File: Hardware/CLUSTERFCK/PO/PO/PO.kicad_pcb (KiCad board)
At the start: 2 copper layers, 2 parts, among them J1 Conn_02x08_Counter_Clockwise, J2 Conn_02x20_Counter_Clockwise

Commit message: 0061|1h|PO Module Versuch 2
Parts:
- J1: value Conn_02x08_Counter_Clockwise -> Conn_02x14_Counter_Clockwise; footprint Connector_PinHeader_2.54mm:PinHeader_2x08_P2.54mm_Vertical_SMD -> Connector_PinHeader_2.54mm:PinHeader_2x14_P2.54mm_Horizontal
- moved J1 19.9 mm to (94.4, 75.1), turned to 0 degrees
- moved J2 0.22 mm to (29.6, 116.7)
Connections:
- J1 pad 1: GND -> /ADDR0
- J1 pad 10: /DATA7 -> /ADDR9
- J1 pad 11: EXT0 -> /ADDR10
- J1 pad 12: EXT1 -> /ADDR11
- J1 pad 13: EXT2 -> HLT
- J1 pad 14: IRPT -> +5V
- J1 pad 15: HLT -> GND
- J1 pad 16: +5V -> CLK
- J1 pad 2: CLK -> /ADDR1
- J1 pad 3: /DATA0 -> /ADDR2
- J1 pad 4: /DATA1 -> /ADDR3
- J1 pad 5: /DATA2 -> /ADDR4
- J1 pad 6: /DATA3 -> /ADDR5
- J1 pad 7: /DATA4 -> /ADDR6
- J1 pad 8: /DATA5 -> /ADDR7
- J1 pad 9: /DATA6 -> /ADDR8
- J2 pad 10: /DATA7 -> DATA
- J2 pad 17: no_connect_31 -> no_connect_30
- J2 pad 18: no_connect_32 -> no_connect_31
- J2 pad 23: /ADDR0 -> /ADDR11
- J2 pad 24: /ADDR1 -> /ADDR10
- J2 pad 25: /ADDR2 -> /ADDR9
- J2 pad 26: /ADDR3 -> /ADDR8
- J2 pad 27: /ADDR4 -> /ADDR7
- J2 pad 28: /ADDR5 -> /ADDR6
- J2 pad 29: /ADDR6 -> /ADDR5
- J2 pad 30: /ADDR7 -> /ADDR4
- J2 pad 31: /ADDR8 -> /ADDR3
- J2 pad 32: /ADDR9 -> /ADDR2
- J2 pad 33: /ADDR10 -> /ADDR1
- J2 pad 34: /ADDR11 -> /ADDR0
- J2 pad 35: no_connect_33 -> no_connect_32
- J2 pad 36: no_connect_34 -> no_connect_33
- J2 pad 37: no_connect_35 -> no_connect_34
- J2 pad 38: no_connect_36 -> no_connect_35
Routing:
- net /DATA7: track 87.3 -> 0.00 mm, vias 2 -> 0
- net DATA: track 0.00 -> 72.5 mm
- net /ADDR6: track 0.00 -> 68.1 mm
- net /ADDR10: track 0.00 -> 68.1 mm
- net /ADDR1: track 0.00 -> 68.0 mm
- net /ADDR8: track 0.00 -> 67.9 mm
- net /ADDR7: track 0.00 -> 67.9 mm
- net /ADDR4: track 0.00 -> 67.9 mm
- net /ADDR3: track 0.00 -> 67.9 mm
- net /ADDR2: track 0.00 -> 67.9 mm
- net /ADDR11: track 0.00 -> 67.9 mm
- net /ADDR9: track 0.00 -> 67.9 mm
- net /ADDR5: track 0.00 -> 67.9 mm
- net /ADDR0: track 0.00 -> 65.7 mm
- net IRPT: track 112.9 -> 78.5 mm, vias 0 -> 1
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- added copper zone on F.Cu, net /ADDR0
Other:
- board outline added: 120.8 x 71.8 mm

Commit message: 0062 | 0 | review PO 2
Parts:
- J1: footprint Connector_PinHeader_2.54mm:PinHeader_2x14_P2.54mm_Horizontal -> Connector_PinHeader_2.54mm:PinHeader_2x14_P2.54mm_Vertical
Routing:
- net /ADDR0: track 65.7 -> 67.9 mm
- removed copper zone on F.Cu, net /ADDR0
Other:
- board text added: "Parallel Output Module"
- board text added: "Tom Schädler 2020"

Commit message: 0063 | 0,1h | PO review 2.1
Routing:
- net /DATA3: track 77.4 -> 76.6 mm
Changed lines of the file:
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@@
   (segment (start 28.1 112.92) (end 80.23 112.92) (width 0.2) (layer "F.Cu") (net 11))
   (segment (start 26.96 111.78) (end 28.1 112.92) (width 0.2) (layer "F.Cu") (net 11))
-  (segment (start 80.23 112.92) (end 80.59 113.28) (width 0.2) (layer "F.Cu") (net 11))
-  (via (at 80.59 113.28) (size 0.43) (drill 0.3) (layers "F.Cu" "B.Cu") (net 11))
+  (via (at 80.23 112.92) (size 0.43) (drill 0.3) (layers "F.Cu" "B.Cu") (net 11))
   (segment (start 95.764999 99.135001) (end 96.94 97.96) (width 0.2) (layer "B.Cu") (net 11))
-  (segment (start 80.6 113.27) (end 80.6 112.560998) (width 0.2) (layer "B.Cu") (net 11))
-  (segment (start 80.59 113.28) (end 80.6 113.27) (width 0.2) (layer "B.Cu") (net 11))
+  (segment (start 80.6 112.560998) (end 80.250998 112.91) (width 0.2) (layer "B.Cu") (net 11))
   (segment (start 80.6 112.560998) (end 94.025997 99.135001) (width 0.2) (layer "B.Cu") (net 11))
   (segment (start 94.025997 99.135001) (end 95.764999 99.135001) (width 0.2) (layer "B.Cu") (net 11))
@@
   (segment (start 26.96 114.32) (end 28.09 115.45) (width 0.2) (layer "B.Cu") (net 13))
   (segment (start 75.170998 115.45) (end 94.025997 96.595001) (width 0.2) (layer "B.Cu") (net 13))
-  (segment (start 25.784999 106.135999) (end 26.585997 105.335001) (width 0.2) (layer "F.Cu") (net 14))
   (segment (start 28.324999 115.495001) (end 26.395999 115.495001) (width 0.2) (layer "F.Cu") (net 14))
   (segment (start 26.395999 115.495001) (end 25.784999 114.884001) (width 0.2) (layer "F.Cu") (net 14))
-  (segment (start 26.585997 105.335001) (end 38.484999 105.335001) (width 0.2) (layer "F.Cu") (net 14))
-  (segment (start 41.98 101.84) (end 87.04 101.84) (width 0.2) (layer "F.Cu") (net 14))
-  (segment (start 87.04 101.84) (end 93.46 95.42) (width 0.2) (layer "F.Cu") (net 14))
+  (segment (start 25.784999 106.135999) (end 26.585997 105.335001) (width 0.2) (layer "F.Cu") (net 14))
+  (segment (start 84.484999 105.335001) (end 87.98 101.84) (width 0.2) (layer "F.Cu") (net 14))
+  (segment (start 87.98 101.84) (end 94.4 95.42) (width 0.2) (layer "F.Cu") (net 14))
+  (segment (start 26.585997 105.335001) (end 84.484999 105.335001) (width 0.2) (layer "F.Cu") (net 14))
+  (segment (start 29.5 114.32) (end 28.324999 115.495001) (width 0.2) (layer "F.Cu") (net 14))
   (segment (start 25.784999 114.884001) (end 25.784999 106.135999) (width 0.2) (layer "F.Cu") (net 14))
-  (segment (start 38.484999 105.335001) (end 41.98 101.84) (width 0.2) (layer "F.Cu") (net 14))
-  (segment (start 93.46 95.42) (end 94.4 95.42) (width 0.25) (layer "F.Cu") (net 14))
-  (segment (start 29.5 114.32) (end 28.324999 115.495001) (width 0.2) (layer "F.Cu") (net 14))
   (segment (start 28.15 100.27) (end 86.35 100.27) (width 0.2) (layer "F.Cu") (net 15))
   (segment (start 95.764999 94.055001) (end 96.94 92.88) (width 0.2) (layer "F.Cu") (net 15))
@@
   (segment (start 29.62 76.04) (end 29.96 76.38) (width 0.2) (layer "F.Cu") (net 33))
   (segment (start 29.96 76.38) (end 95.66 76.38) (width 0.2) (layer "F.Cu") (net 33))
-  (segment (start 92.3 74.89) (end 92.51 75.1) (width 0.2) (layer "F.Cu") (net 34))
-  (segment (start 28.230001 74.889999) (end 92.299999 74.889999) (width 0.2) (layer "F.Cu") (net 34))
-  (segment (start 92.299999 74.889999) (end 92.3 74.89) (width 0.2) (layer "F.Cu") (net 34))
-  (segment (start 92.51 75.1) (end 94.4 75.1) (width 0.2) (layer "F.Cu") (net 34))
+  (segment (start 94.189999 74.889999) (end 94.4 75.1) (width 0.2) (layer "F.Cu") (net 34))
   (segment (start 27.08 76.04) (end 28.230001 74.889999) (width 0.2) (layer "F.Cu") (net 34))
+  (segment (start 28.230001 74.889999) (end 94.189999 74.889999) (width 0.2) (layer "F.Cu") (net 34))
   (zone (net 16) (net_name "GND") (layer "B.Cu") (hatch edge 0.508)
     (connect_pads (clearance 0.508))

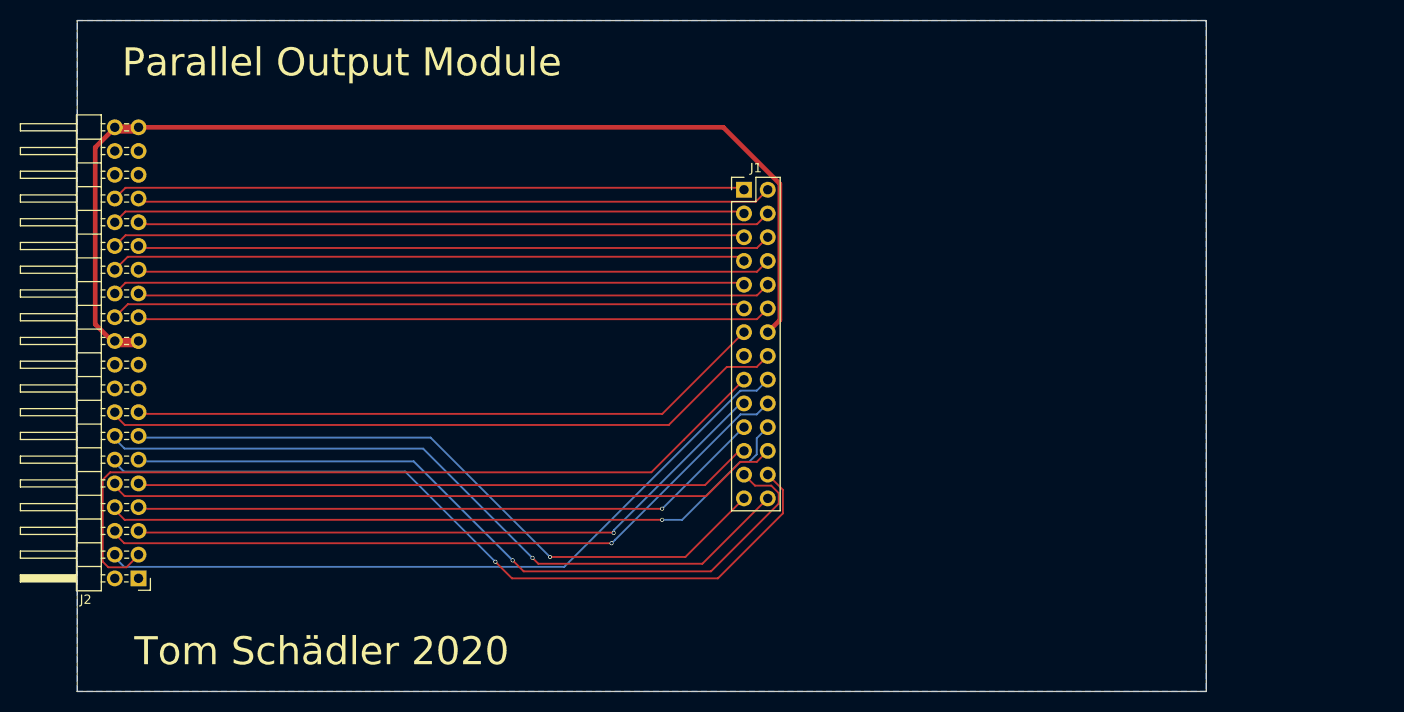
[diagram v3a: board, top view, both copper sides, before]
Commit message: quickfix PO width
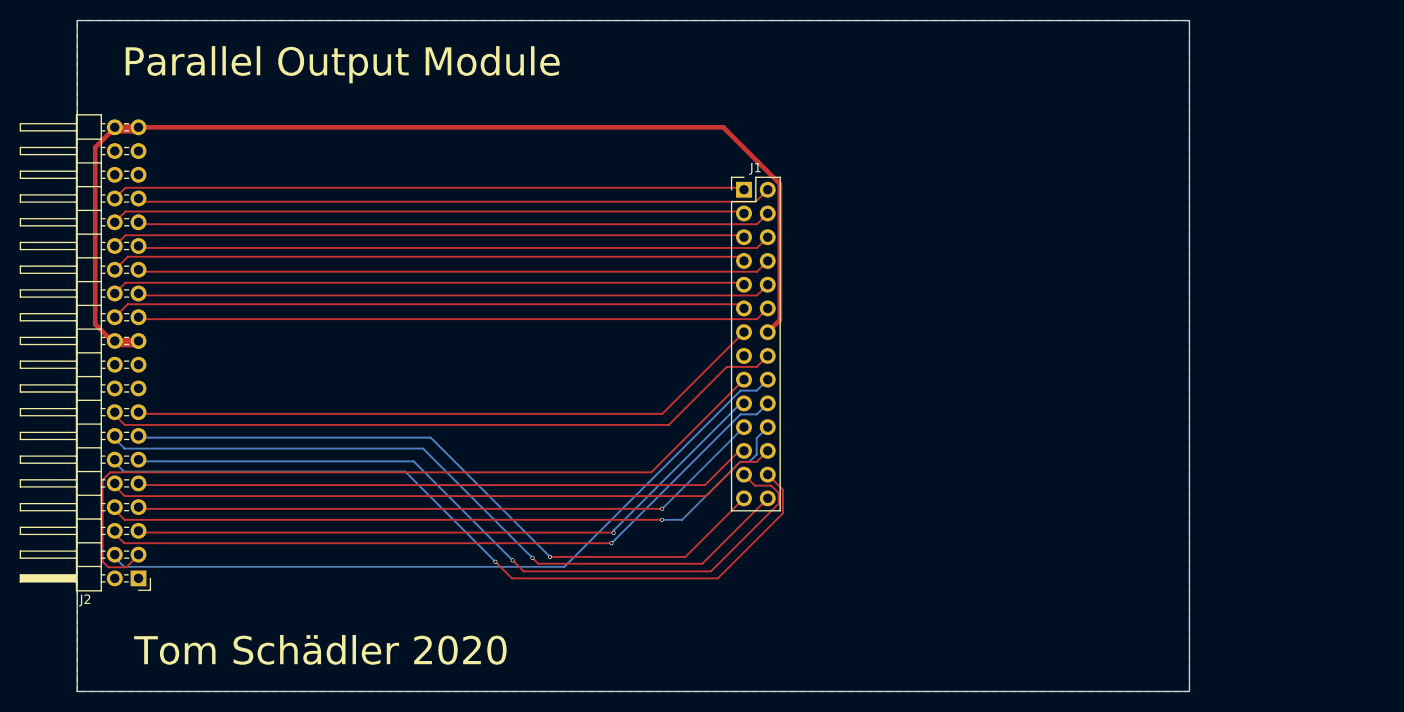
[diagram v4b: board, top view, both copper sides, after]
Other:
- board size 120.8 x 71.8 mm -> 119 x 71.8 mm
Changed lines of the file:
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@@
     )
   )
-  (gr_line (start 143.86 128.78) (end 143.86 57) (layer "Edge.Cuts") (width 0.1))
-  (gr_line (start 143.86 57) (end 23.06 57) (layer "Edge.Cuts") (width 0.1))
+  (gr_line (start 142.06 128.78) (end 142.06 57) (layer "Edge.Cuts") (width 0.1))
+  (gr_line (start 23.06 57) (end 142.06 57) (layer "Edge.Cuts") (width 0.1))
   (gr_line (start 23.06 57) (end 23.06 128.78) (layer "Edge.Cuts") (width 0.1))
-  (gr_line (start 23.06 128.78) (end 143.86 128.78) (layer "Edge.Cuts") (width 0.1))
+  (gr_line (start 23.06 128.78) (end 142.06 128.78) (layer "Edge.Cuts") (width 0.1))
   (gr_text "Tom Schädler 2020" (at 49.225 124.475) (layer "F.SilkS")
     (effects (font (size 3 3) (thickness 0.4)))
@@
     (polygon
       (pts
-        (xy 143.86 128.78)
+        (xy 142.06 128.78)
         (xy 23.06 128.78)
         (xy 23.06 57)
-        (xy 143.86 57)
+        (xy 142.06 57)
       )
     )

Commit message: 0066 | 6h | made holes in pcbs
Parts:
- added REF**: MountingHole_4.3mm_M4, MountingHole:MountingHole_4.3mm_M4, F.Cu at (52.9, 61.1)
- added REF**: MountingHole_4.3mm_M4, MountingHole:MountingHole_4.3mm_M4, F.Cu at (136.7, 62.3)
- added REF**: MountingHole_4.3mm_M4, MountingHole:MountingHole_4.3mm_M4, F.Cu at (28.6, 123.5)
- added REF**: MountingHole_4.3mm_M4, MountingHole:MountingHole_4.3mm_M4, F.Cu at (136.7, 123.5)
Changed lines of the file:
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@@
   (net 33 "/ADDR1")
   (net 34 "/ADDR0")
+  (footprint "MountingHole:MountingHole_4.3mm_M4" (layer "F.Cu")
+    (at 52.86 61.08)
+    (descr "Mounting Hole 4.3mm, no annular, M4")
+    (tags "mounting hole 4.3mm no annular m4")
+    (attr exclude_from_pos_files exclude_from_bom)
+    (fp_text reference "REF**" (at 0.09 -2.93) (layer "F.SilkS")
+      (effects (font (size 1 1) (thickness 0.15)))
+    )
+    (fp_text value "MountingHole_4.3mm_M4" (at 0 5.3) (layer "F.Fab")
+      (effects (font (size 1 1) (thickness 0.15)))
+    )
+    (fp_text user "${REFERENCE}" (at 0.3 0) (layer "F.Fab")
+      (effects (font (size 1 1) (thickness 0.15)))
+    )
+    (fp_circle (center 0 0) (end 4.3 0) (layer "Cmts.User") (width 0.15) (fill none))
+    (fp_circle (center 0 0) (end 4.55 0) (layer "F.CrtYd") (width 0.05) (fill none))
+    (pad "1" np_thru_hole circle (at 0 0) (size 4.3 4.3) (drill 4.3) (layers *.Cu *.Mask))
+  )
+  (footprint "MountingHole:MountingHole_4.3mm_M4" (layer "F.Cu")
+    (at 136.66 62.31)
+    (descr "Mounting Hole 4.3mm, no annular, M4")
+    (tags "mounting hole 4.3mm no annular m4")
+    (attr exclude_from_pos_files exclude_from_bom)
+    (fp_text reference "REF**" (at 0.09 -2.93) (layer "F.SilkS")
+      (effects (font (size 1 1) (thickness 0.15)))
+    )
+    (fp_text value "MountingHole_4.3mm_M4" (at 0 5.3) (layer "F.Fab")
+      (effects (font (size 1 1) (thickness 0.15)))
+    )
+    (fp_text user "${REFERENCE}" (at 0.3 0) (layer "F.Fab")
+      (effects (font (size 1 1) (thickness 0.15)))
+    )
+    (fp_circle (center 0 0) (end 4.3 0) (layer "Cmts.User") (width 0.15) (fill none))
+    (fp_circle (center 0 0) (end 4.55 0) (layer "F.CrtYd") (width 0.05) (fill none))
+    (pad "1" np_thru_hole circle (at 0 0) (size 4.3 4.3) (drill 4.3) (layers *.Cu *.Mask))
+  )
   (footprint "Connector_PinHeader_2.54mm:PinHeader_2x14_P2.54mm_Vertical" (layer "F.Cu")
     (at 94.4 75.1)
@@
     )
   )
+  (footprint "MountingHole:MountingHole_4.3mm_M4" (layer "F.Cu")
+    (at 28.61 123.46)
+    (descr "Mounting Hole 4.3mm, no annular, M4")
+    (tags "mounting hole 4.3mm no annular m4")
+    (attr exclude_from_pos_files exclude_from_bom)
+    (fp_text reference "REF**" (at 0.09 -2.93) (layer "F.SilkS")
+      (effects (font (size 1 1) (thickness 0.15)))
+    )
+    (fp_text value "MountingHole_4.3mm_M4" (at 0 5.3) (layer "F.Fab")
+      (effects (font (size 1 1) (thickness 0.15)))
+    )
+    (fp_text user "${REFERENCE}" (at 0.3 0) (layer "F.Fab")
+      (effects (font (size 1 1) (thickness 0.15)))
+    )
+    (fp_circle (center 0 0) (end 4.3 0) (layer "Cmts.User") (width 0.15) (fill none))
+    (fp_circle (center 0 0) (end 4.55 0) (layer "F.CrtYd") (width 0.05) (fill none))
+    (pad "1" np_thru_hole circle (at 0 0) (size 4.3 4.3) (drill 4.3) (layers *.Cu *.Mask))
+  )
+  (footprint "MountingHole:MountingHole_4.3mm_M4" (layer "F.Cu")
+    (at 136.66 123.46)
+    (descr "Mounting Hole 4.3mm, no annular, M4")
+    (tags "mounting hole 4.3mm no annular m4")
+    (attr exclude_from_pos_files exclude_from_bom)
+    (fp_text reference "REF**" (at 0.09 -2.93) (layer "F.SilkS")
+      (effects (font (size 1 1) (thickness 0.15)))
+    )
+    (fp_text value "MountingHole_4.3mm_M4" (at 0 5.3) (layer "F.Fab")
+      (effects (font (size 1 1) (thickness 0.15)))
+    )
+    (fp_text user "${REFERENCE}" (at 0.3 0) (layer "F.Fab")
+      (effects (font (size 1 1) (thickness 0.15)))
+    )
+    (fp_circle (center 0 0) (end 4.3 0) (layer "Cmts.User") (width 0.15) (fill none))
+    (fp_circle (center 0 0) (end 4.55 0) (layer "F.CrtYd") (width 0.05) (fill none))
+    (pad "1" np_thru_hole circle (at 0 0) (size 4.3 4.3) (drill 4.3) (layers *.Cu *.Mask))
+  )
   (gr_line (start 142.06 128.78) (end 142.06 57) (layer "Edge.Cuts") (width 0.1))
   (gr_line (start 23.06 57) (end 142.06 57) (layer "Edge.Cuts") (width 0.1))
   (gr_line (start 23.06 57) (end 23.06 128.78) (layer "Edge.Cuts") (width 0.1))
   (gr_line (start 23.06 128.78) (end 142.06 128.78) (layer "Edge.Cuts") (width 0.1))
-  (gr_text "Tom Schädler 2020" (at 49.225 124.475) (layer "F.SilkS")
+  (gr_text "Tom Schädler 2020" (at 56.86 123.12) (layer "F.SilkS")
     (effects (font (size 3 3) (thickness 0.4)))
   )
-  (gr_text "Parallel Output Module" (at 51.375 61.475) (layer "F.SilkS")
-    (effects (font (size 3 3) (thickness 0.4)))
+  (gr_text "Parallel Output Module" (at 60.46 61.31) (layer "F.SilkS")
+    (effects (font (size 4 4) (thickness 0.6)))
   )
   (segment (start 98.240001 74.475999) (end 92.184002 68.42) (width 0.5) (layer "F.Cu") (net 1))

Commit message: 0072 | 3h | make silkscreen prettier
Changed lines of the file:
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@@
     (effects (font (size 3 3) (thickness 0.4)))
   )
-  (gr_text "Parallel Output Module" (at 60.46 61.31) (layer "F.SilkS")
+  (gr_text "Parallel Output Module" (at 94.9 61.575) (layer "F.SilkS")
     (effects (font (size 4 4) (thickness 0.6)))
   )
